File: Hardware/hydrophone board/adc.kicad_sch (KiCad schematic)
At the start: 34 parts, among them X401 ASE-xxxMHz

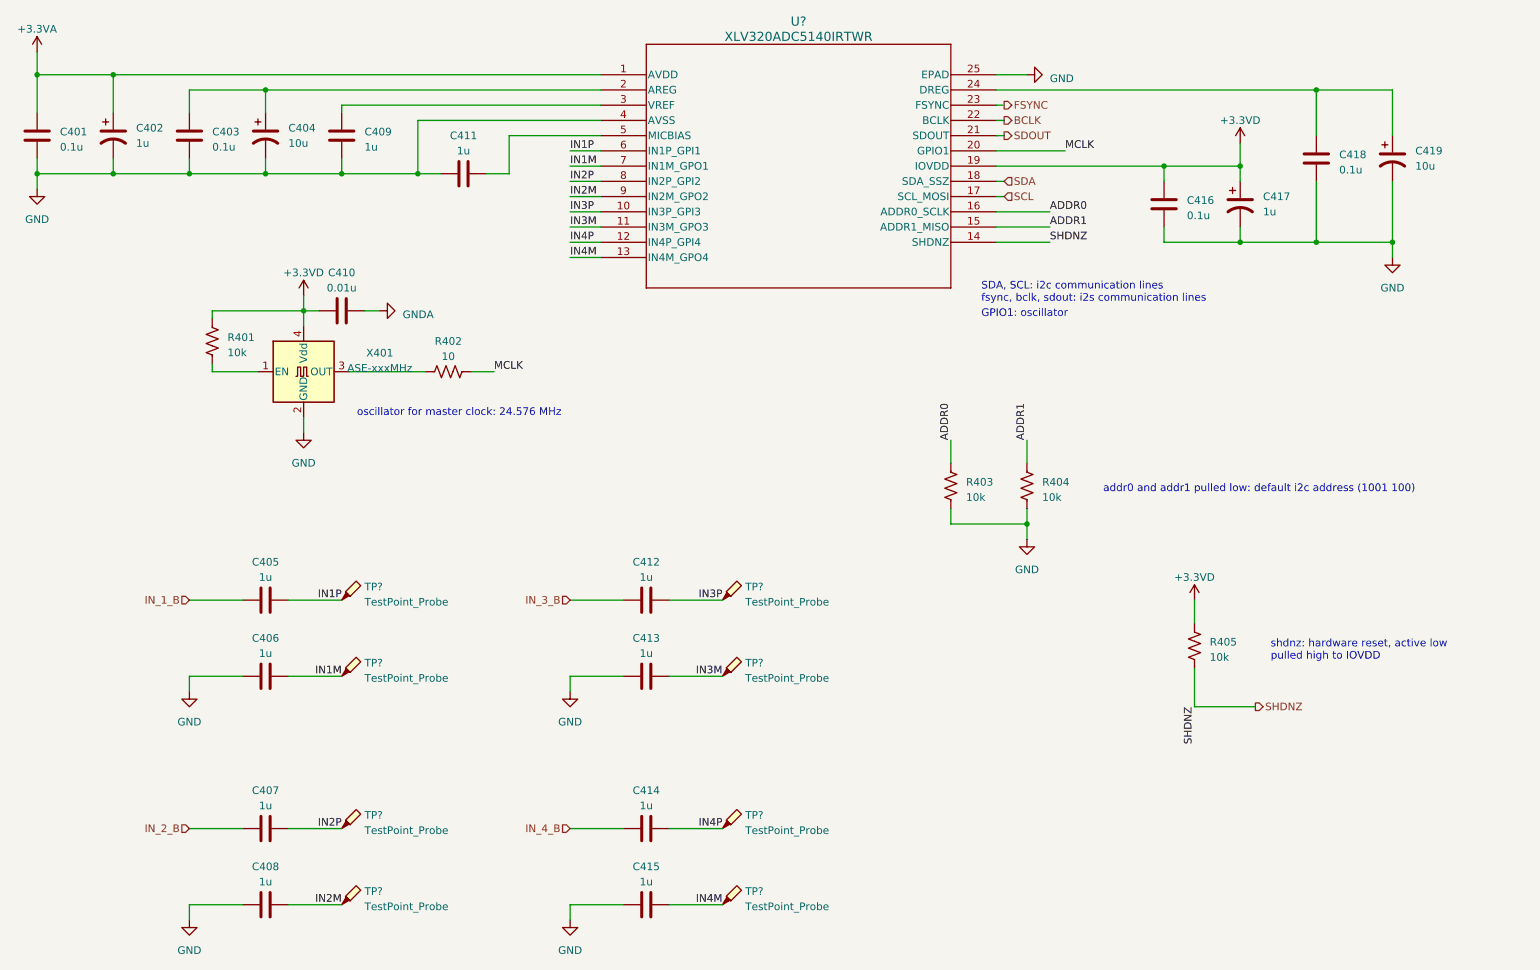
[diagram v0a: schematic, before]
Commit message: added teensy footprint
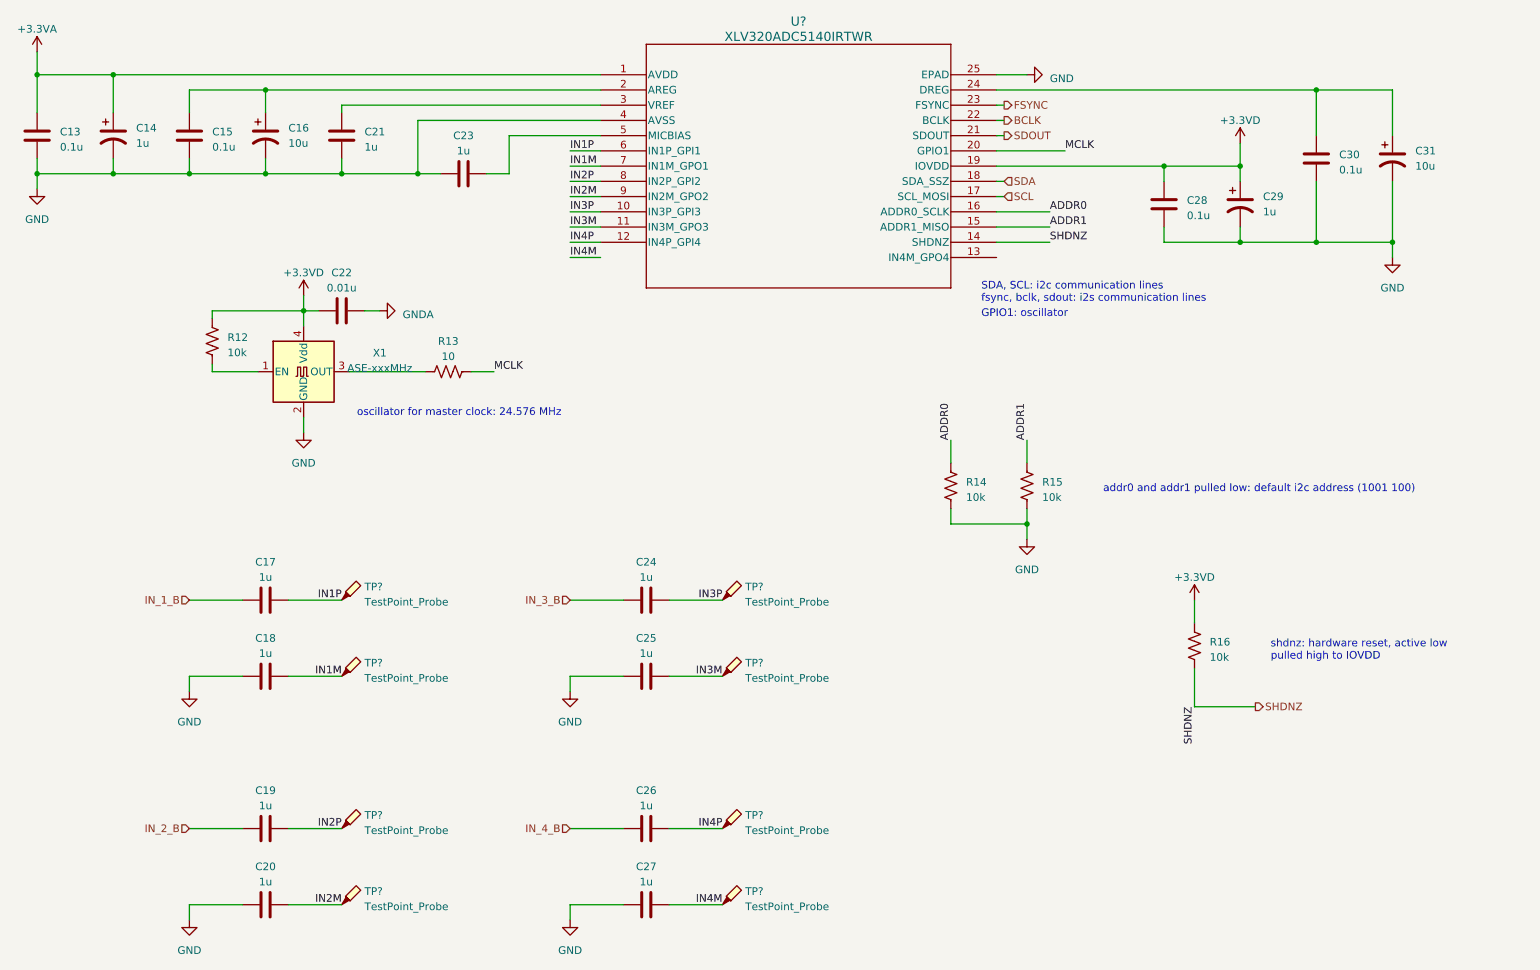
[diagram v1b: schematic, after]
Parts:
- U?: footprint RTW24_4P15X4P15_TEX -> TLV320ADC5140:RTW24_4P15X4P15_TEX
- renumbered C401 to C13, C402 to C14, C403 to C15, C404 to C16, C405 to C17, C406 to C18, C407 to C19, C408 to C20, C409 to C21, C410 to C22, C411 to C23, C412 to C24, C413 to C25, C414 to C26, C415 to C27, C416 to C28, C417 to C29, C418 to C30, C419 to C31, R401 to R12, R402 to R13, R403 to R14, R404 to R15, R405 to R16, X401 to X1
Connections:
- net IN4M: no longer U?.13 (IN4M_GPO4)

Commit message: Update adc.kicad_sch
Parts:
- removed C22: 0.01u, symbol Device:C
- removed R12: 10k, symbol Device:R_US
- removed R13: 10, symbol Device:R_US
- removed X1: ASE-xxxMHz, Oscillator:Oscillator_SMD_Abracon_ASE-4Pin_3.2x2.5mm, symbol Oscillator:ASE-xxxMHz
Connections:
- net IN4M: now also U?.13 (IN4M_GPO4)
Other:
- note added: "- add pull ups for i2c - connect schndz + gpio1 to teensy"
- note removed: "oscillator for master clock: 24.576 MHz"

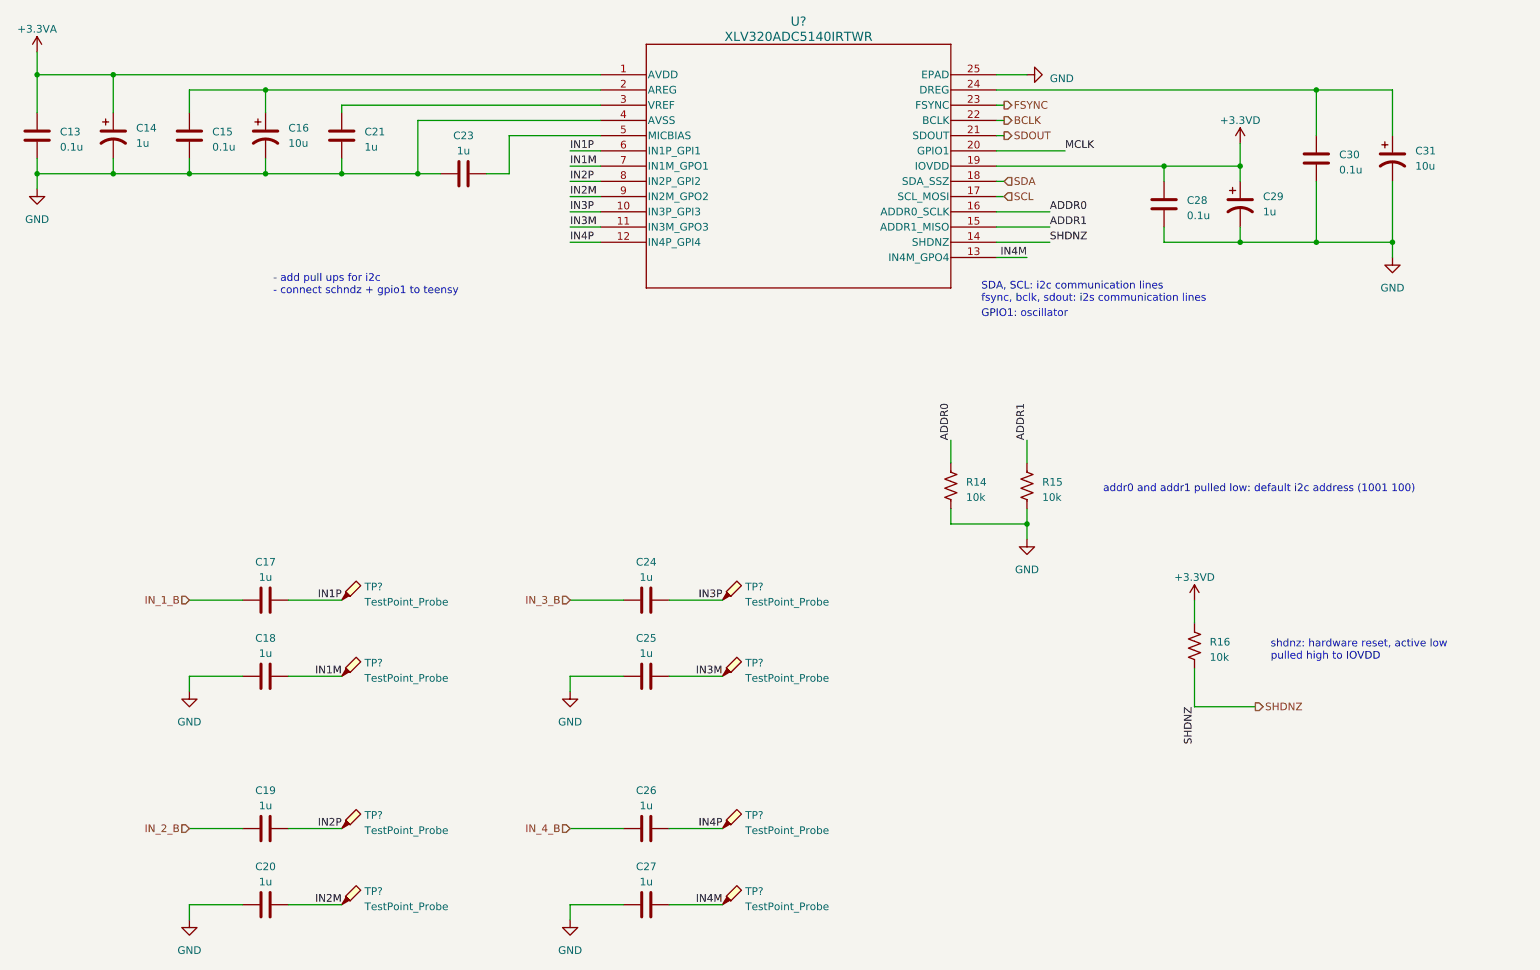
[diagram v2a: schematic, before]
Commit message: i2c pull ups
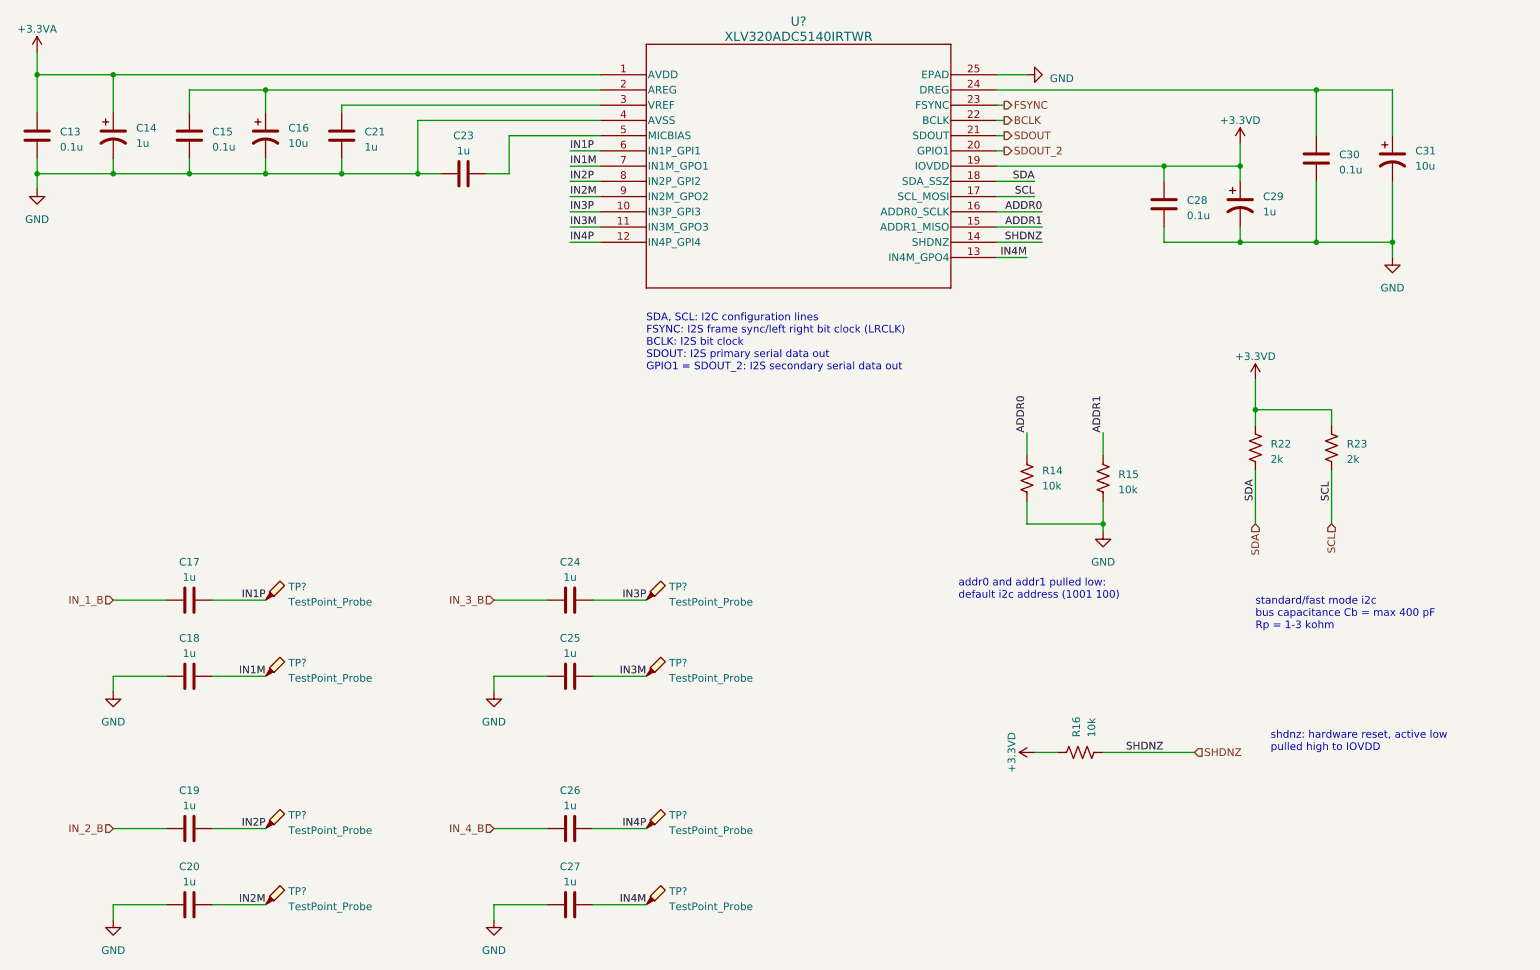
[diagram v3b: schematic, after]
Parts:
- added R22, R23: 2k, symbol Device:R_US
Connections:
- net +3.3VD: now also R22.1, R23.1
- net ADDR0: now also R14.2; no longer R14.1
- net GND: now also R14.1; no longer R14.2
- net SCL: now also R23.2
- net SDA: now also R22.2
- net MCLK renamed SDOUT_2
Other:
- note added: "SDA, SCL: I2C configuration lines FSYNC: I2S frame sync/left right bit clock (LRCLK) BCLK: I2S bit clock SDOUT: I2S primary serial data out GPIO1 = SDOUT_2: I2S secondary serial data out"
- note added: "standard/fast mode i2c bus capacitance Cb = max 400 pF Rp = 1-3 kohm"
- note removed: "- add pull ups for i2c - connect schndz + gpio1 to teensy"
- note removed: "GPIO1: oscillator"
- note removed: "SDA, SCL: i2c communication lines fsync, bclk, sdout: i2s communication lines"
- moved on the sheet: C17, C18, C19, C20, C24, C25, C26, C27, R14, R15, R16, TP?

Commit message: changed connectors
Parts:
- R14, R15, R16: value 10k -> 1k
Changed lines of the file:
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@@
       (effects (font (size 1.27 1.27)) (justify right))
     )
-    (property "Value" "10k" (at 193.04 107.95 0)
+    (property "Value" "1k" (at 193.04 107.95 0)
       (effects (font (size 1.27 1.27)) (justify right))
     )
@@
       (effects (font (size 1.27 1.27)) (justify left))
     )
-    (property "Value" "10k" (at 205.74 108.585 0)
+    (property "Value" "1k" (at 205.74 108.585 0)
       (effects (font (size 1.27 1.27)) (justify left))
     )
@@
       (effects (font (size 1.27 1.27)) (justify left))
     )
-    (property "Value" "10k" (at 201.295 149.86 0)
-      (effects (font (size 1.27 1.27)) (justify left))
-    )
+    (property "Value" "1k" (at 201.295 149.86 0)
+      (effects (font (size 1.27 1.27)) (justify left))
+    )

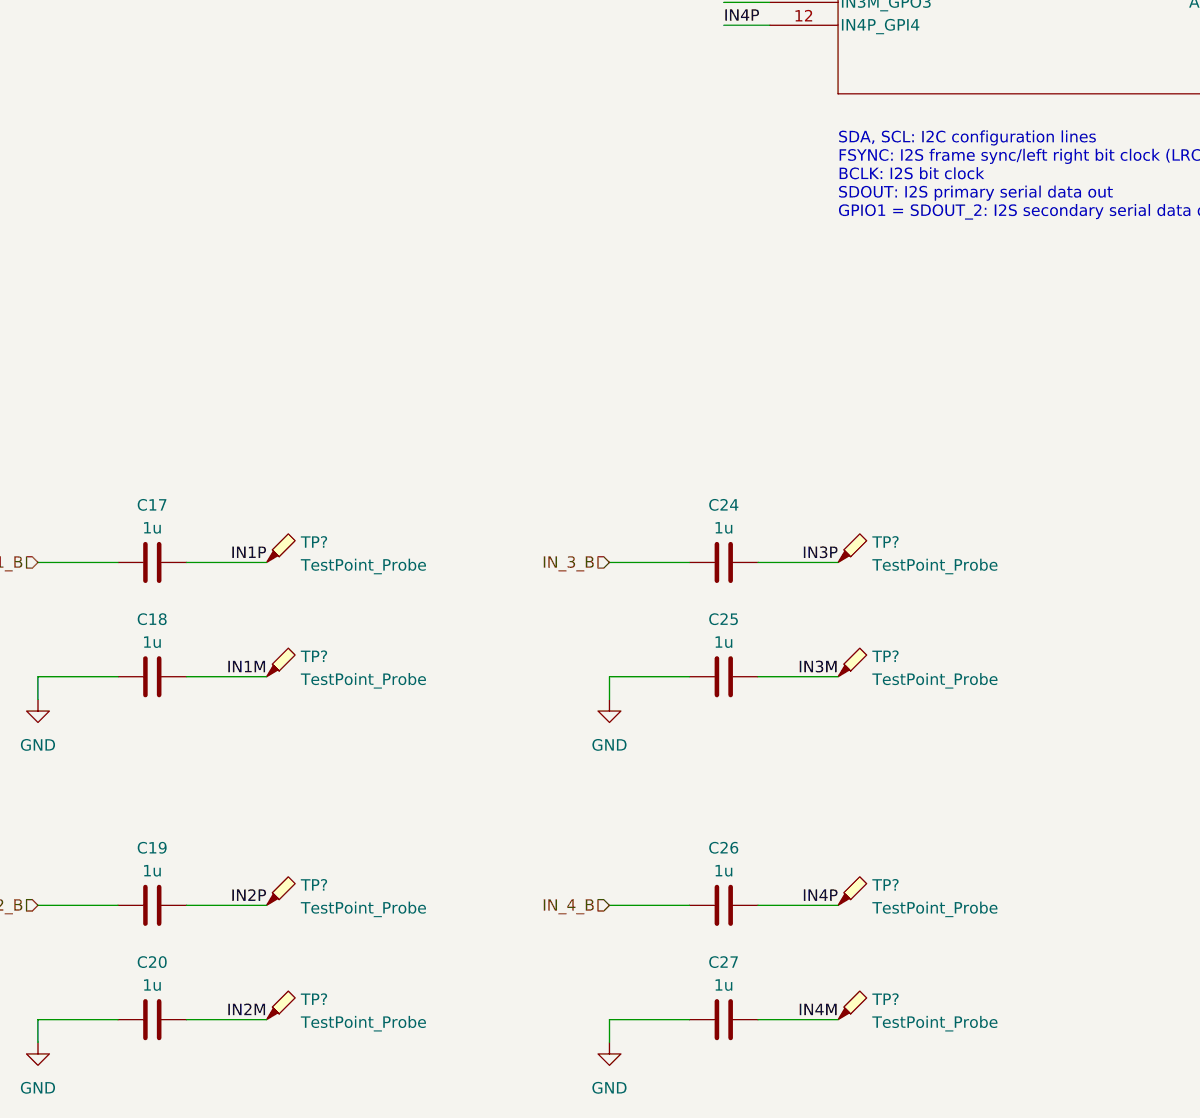
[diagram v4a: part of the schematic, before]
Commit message: removed some connectors
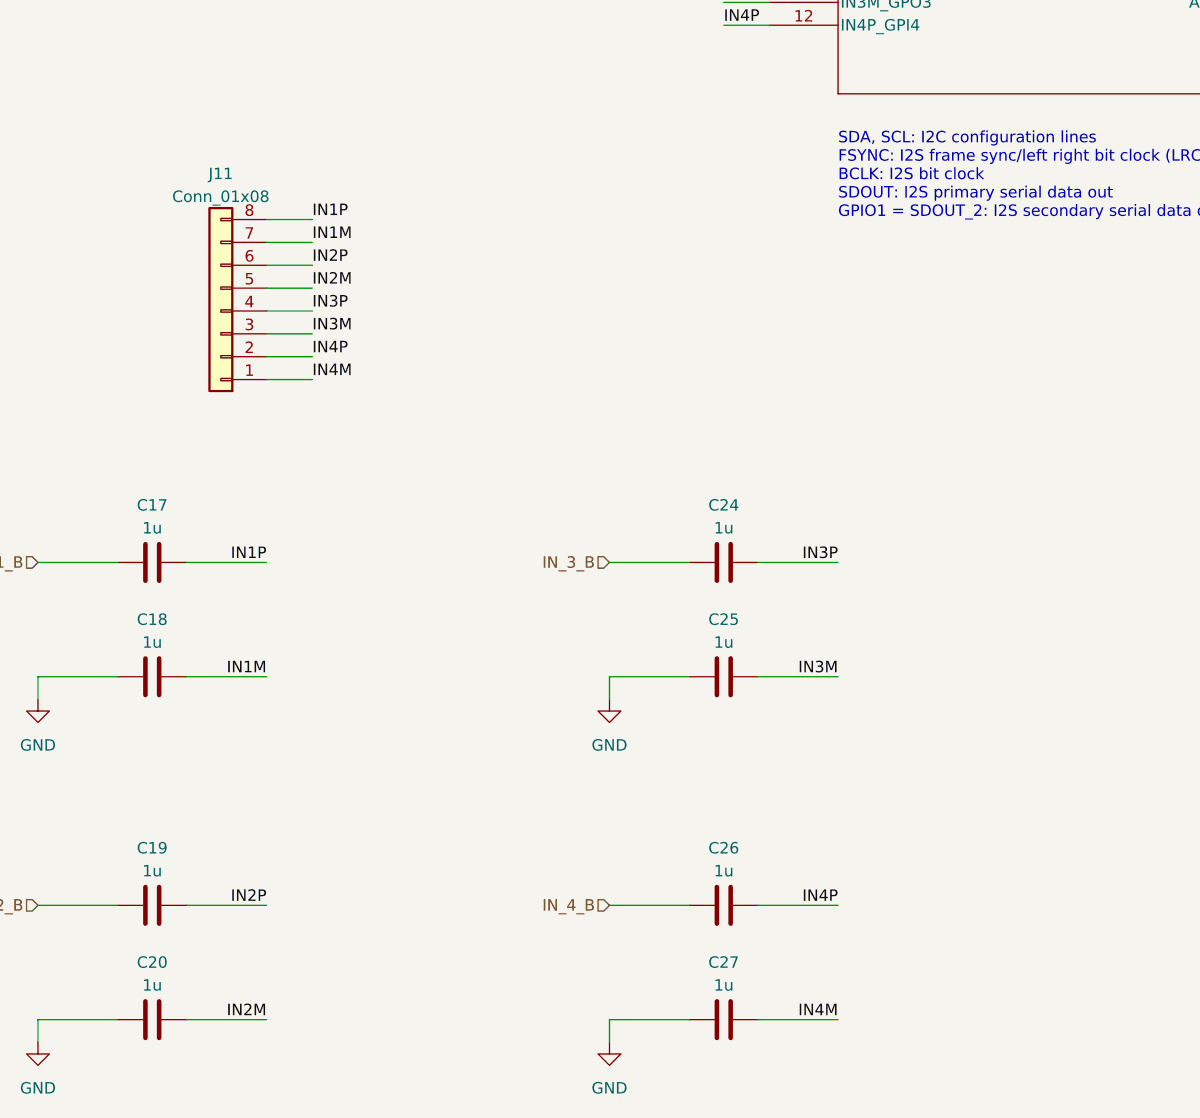
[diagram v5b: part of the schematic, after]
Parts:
- removed TP? (x8): TestPoint_Probe, symbol Connector:TestPoint_Probe
- added J11: Conn_01x08, symbol Connector_Generic:Conn_01x08
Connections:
- net IN1M: now also J11.7 (Pin_7)
- net IN1P: now also J11.8 (Pin_8)
- net IN2M: now also J11.5 (Pin_5)
- net IN2P: now also J11.6 (Pin_6)
- net IN3M: now also J11.3 (Pin_3)
- net IN3P: now also J11.4 (Pin_4)
- net IN4M: now also J11.1 (Pin_1)
- net IN4P: now also J11.2 (Pin_2)

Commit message: annotate all component
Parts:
- renumbered C13 to C1101, C14 to C1102, C15 to C1103, C17 to C1104, C18 to C1105, C19 to C1106, C20 to C1107, C16 to C1108, C21 to C1109, C23 to C1110, C24 to C1111, C25 to C1112, C26 to C1113, C27 to C1114, C28 to C1115, C29 to C1116, C30 to C1117, C31 to C1118, J11 to J1101, R14 to R1101, R16 to R1102, R15 to R1103, R22 to R1104, R23 to R1105

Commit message: assigned footprints
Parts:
- C301: renamed from C1101; footprint (none) -> Capacitor_SMD:C_0603_1608Metric
- C302: renamed from C1102; footprint (none) -> Capacitor_SMD:C_0603_1608Metric
- C303: renamed from C1103; footprint (none) -> Capacitor_SMD:C_0603_1608Metric
- C304: renamed from C1108; footprint (none) -> Capacitor_SMD:C_0805_2012Metric
- C305: renamed from C1109; footprint (none) -> Capacitor_SMD:C_0603_1608Metric
- C306: renamed from C1117; footprint (none) -> Capacitor_SMD:C_0603_1608Metric
- C307: renamed from C1118; footprint (none) -> Capacitor_SMD:C_0805_2012Metric
- C308: renamed from C1110; footprint (none) -> Capacitor_SMD:C_0603_1608Metric
- C309: renamed from C1115; footprint (none) -> Capacitor_SMD:C_0603_1608Metric
- C310: renamed from C1116; footprint (none) -> Capacitor_SMD:C_0603_1608Metric
- C311: renamed from C1104; footprint (none) -> Capacitor_SMD:C_0603_1608Metric
- C312: renamed from C1111; footprint (none) -> Capacitor_SMD:C_0603_1608Metric
- C313: renamed from C1105; footprint (none) -> Capacitor_SMD:C_0603_1608Metric
- C314: renamed from C1112; footprint (none) -> Capacitor_SMD:C_0603_1608Metric
- C315: renamed from C1106; footprint (none) -> Capacitor_SMD:C_0603_1608Metric
- C316: renamed from C1113; footprint (none) -> Capacitor_SMD:C_0603_1608Metric
- C317: renamed from C1107; footprint (none) -> Capacitor_SMD:C_0603_1608Metric
- C318: renamed from C1114; footprint (none) -> Capacitor_SMD:C_0603_1608Metric
- J301: renamed from J1101; footprint (none) -> Connector_PinSocket_2.54mm:PinSocket_1x08_P2.54mm_Vertical
- R301: renamed from R1104; footprint (none) -> Resistor_SMD:R_0603_1608Metric
- R302: renamed from R1105; footprint (none) -> Resistor_SMD:R_0603_1608Metric
- R303: renamed from R1101; footprint (none) -> Resistor_SMD:R_0603_1608Metric
- R304: renamed from R1103; footprint (none) -> Resistor_SMD:R_0603_1608Metric
- R305: renamed from R1102; footprint (none) -> Resistor_SMD:R_0603_1608Metric
